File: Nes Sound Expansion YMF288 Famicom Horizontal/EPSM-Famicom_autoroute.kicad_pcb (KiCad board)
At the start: 2 copper layers, 99 x 91.7 mm, 68 parts, among them J1 CARTRIDGE_F, J2 CONSOLE_M, J3 AudioJack4_SwitchTR1, U1 74HC688, U10 74HC132, U11 74HC257, U12 74HC257, U13 LM358, U14 74LVC1G373, U15 74HC257, U2 74HC139, U3 74HC174, U4 74HC174, U5 74HC688, U6 74HC688, U7 74HC132, U8 YMF288, U9 BU9480F, X1 SG-8002CA

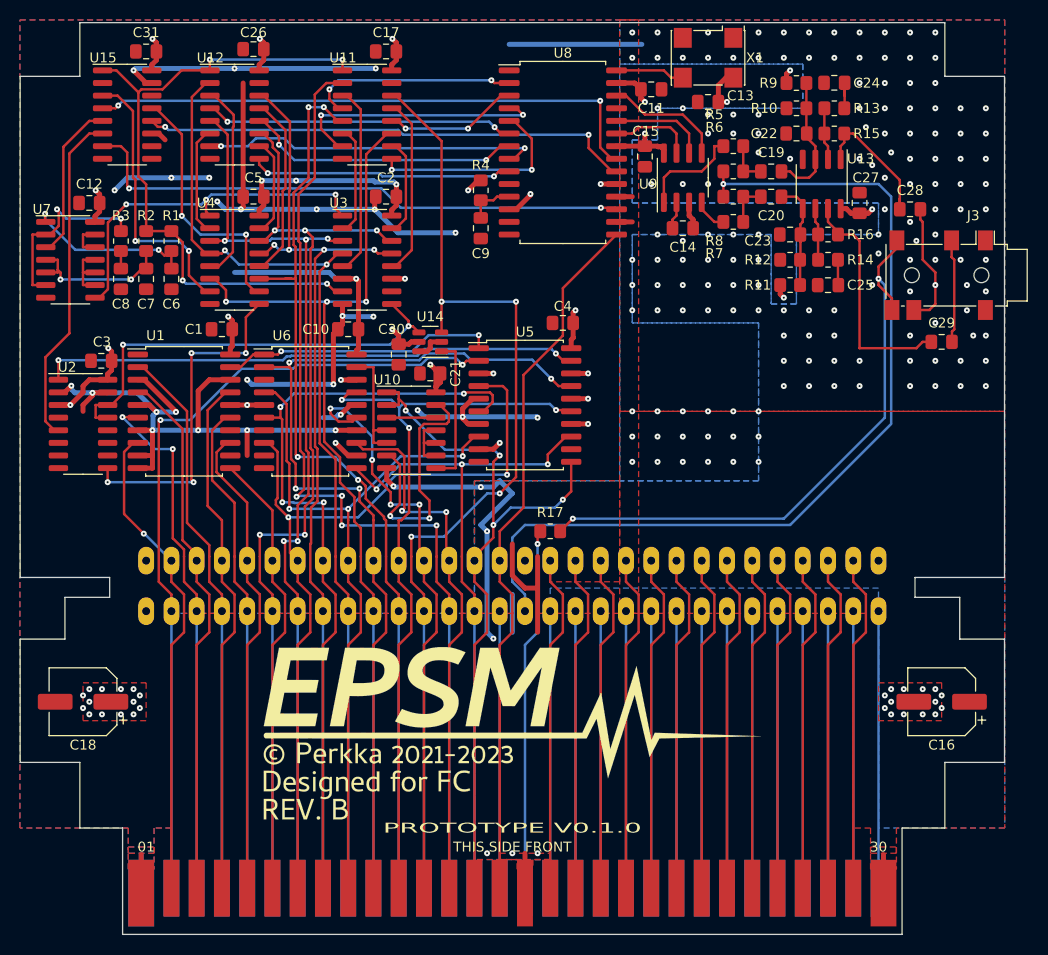
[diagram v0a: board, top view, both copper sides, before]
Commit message: Improved routing
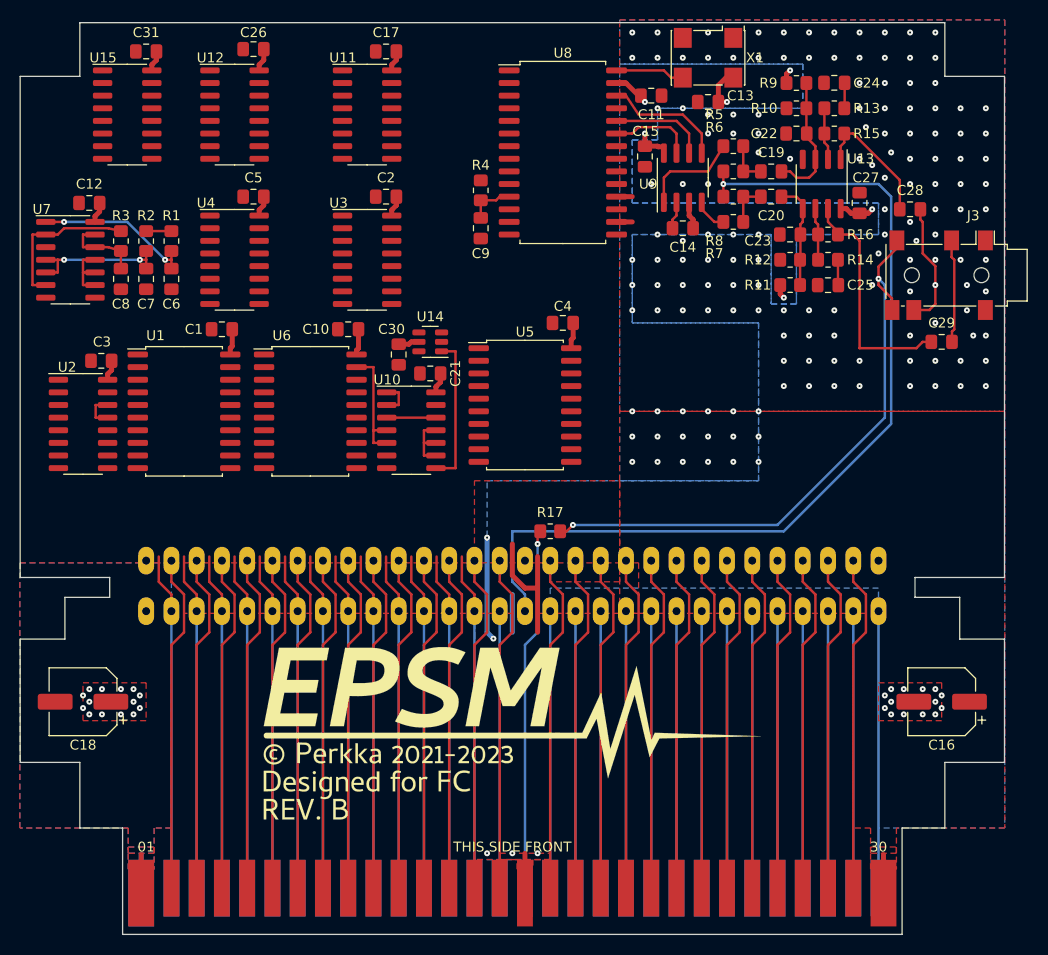
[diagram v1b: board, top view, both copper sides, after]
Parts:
- moved C11 0.64 mm to (141.0, 53.3)
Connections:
- U7 pad 12: Net-(U7-Pad12) -> Net-(C8-Pad1)
- U7 pad 13: Net-(U7-Pad12) -> Net-(C8-Pad1)
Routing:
- net GND: track 260.4 -> 41.9 mm, vias 179 -> 152
- net VCC: track 142.7 -> 52.3 mm, vias 65 -> 38
- net /CPU_D1: track 100.2 -> 33.9 mm, vias 4 -> 0
- net /CPU_D0: track 99.1 -> 33.9 mm, vias 4 -> 0
- net /$4016_EN: track 66.9 -> 2.54 mm, vias 4 -> 0
- net /CPU_D4: track 97.9 -> 33.9 mm, vias 2 -> 0
- net /CPU_D7: track 97.3 -> 33.9 mm, vias 5 -> 0
- net /CPU_D3: track 96.8 -> 33.9 mm, vias 3 -> 0
- net /CPU_D5: track 96.7 -> 33.9 mm, vias 4 -> 0
- net /CPU_D6: track 94.5 -> 33.9 mm, vias 5 -> 0
- net /CPU_D2: track 94.1 -> 33.9 mm, vias 4 -> 0
- net /CPU_A3: track 93.8 -> 34.0 mm, vias 4 -> 0
- net /YM_A1: track 57.2 -> 0.00 mm, vias 2 -> 0
- net /YM_CS: track 56.3 -> 0.00 mm, vias 2 -> 0
- net /$401x_~{CE}: track 54.5 -> 0.00 mm, vias 2 -> 0
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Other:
- board text removed: "PROTOTYPE V0.1.0"
